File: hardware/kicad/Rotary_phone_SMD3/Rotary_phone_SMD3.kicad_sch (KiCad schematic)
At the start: 76 parts, among them J1 Barrel_Jack_PTH_Slot, J10 RJ12, J11 PINHD_1x2_Male, J12 PINHD_1x3_Male, J13 PINHD_1x2_Male, J2 PINHD_1x2_Male, J3 PINHD_1x2_Male, J4 PINHD_1x2_Male, J5 PINHD_1x2_Male, J6 PINHD_1x2_Male, J7 PINHD_1x2_Male, J8 PINHD_1x2_Male, J9 RJ12, U1 ME6211C33M5G-N, U2 ESP32-C6-WROOM-1, U3 USBLC6-2SC6, U4 ES8388, U5 AG1171, U6 AG1171

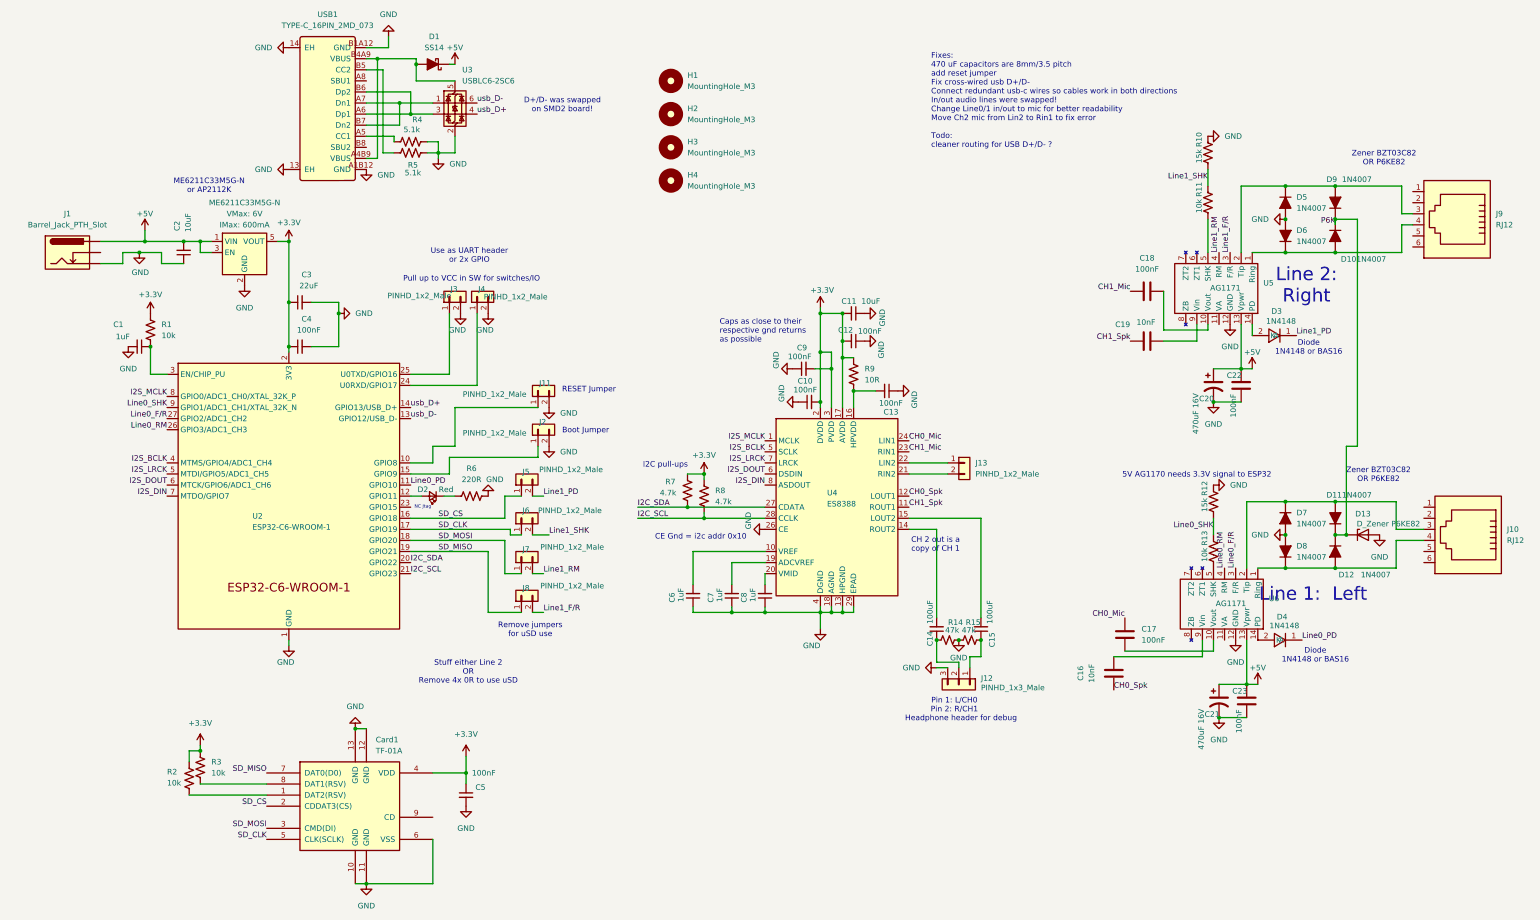
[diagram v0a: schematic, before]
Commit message: 211 recording rework, activity log, ag1170 pulse-debounce fix, SMD4 board, public docs pass
Firmware:
- ag1170: require a minimum loop-open duration (pulse_break_min_ms=15) for a
  rotary pulse to count, not just a maximum -- fixes a ~3-5ms mechanical
  contact-bounce glitch occasionally being miscounted as an extra pulse
  (confirmed live: "211" misread as "212"/"322").
- 211 recording: drop the escalating warning-beep sequence in favor of just
  ending the recording silently; default max length raised 30s -> 2min
  (still user-adjustable, capped at BOARD_RECORD_MAX_MS_MAX); recorder AGC
  with a per-block hard ceiling to stop a startup transient from clipping;
  8s trailing-silence auto-stop kept from the previous tuning pass.
- Recordings/storage lists now sort newest-first.
- sdcard: optional card-detect (CD) pin support, wired up for SMD4 (inert on
  boards without BOARD_SD_CD defined).
- New `activity` component: small ring buffer of human-readable recent
  events (calls, recordings, dial errors) for the Status page, independent
  of the raw debug log.
- webui: dial-code/guide cards moved onto the Status page; the raw debug log
  panel moved to the Diagnostics tab (Settings), next to the log-level
  controls it belongs with.
- voip: retire the voip_provisioner auto-provisioning companion service in
  favor of a plain per-board setup password (gates /api/prompt_requests for
  gen_prompt.py --sync); ships with no default SIP server/hostname baked in.
- dialplan: drop four novelty dial-code clips whose source audio never
  shipped in this checkout (burp/dial-up modem remain).

Hardware:
- Add the SMD4 KiCad project (SMD3's schematic re-routed as a 2-layer
  board); add a 3d-printed-case doc stub.
- Drop SMD3's fab-output cruft (gerbers, DRC/ERC reports, JLCImport
  libraries, BOM) from tracking -- regenerable, and JLCImport in particular
  carries machine-local absolute paths. .gitignore now covers this class of
  file for every board going forward instead of one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
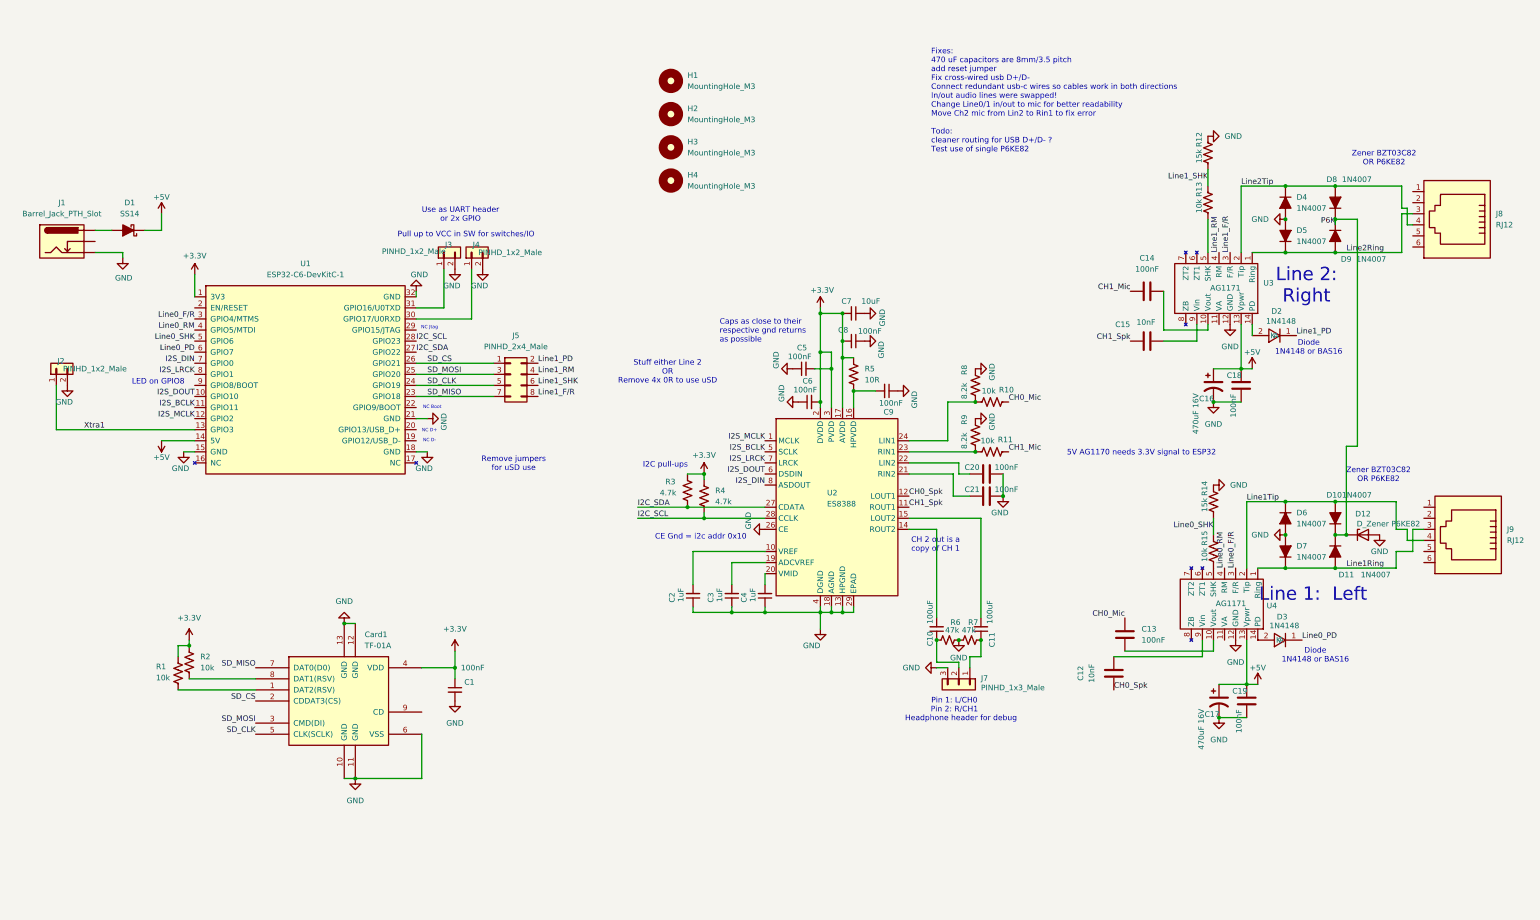
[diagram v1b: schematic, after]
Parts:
- removed C1: 1uF, Capacitor_SMD:C_0402_1005Metric, symbol PCM_SparkFun-Capacitor:C_Small
- removed C2: 10uF, Capacitor_SMD:C_0402_1005Metric, symbol PCM_SparkFun-Capacitor:C_Small
- removed C3: 22uF, PCM_SparkFun-Capacitor:C_0603_1608Metric, symbol PCM_SparkFun-Capacitor:C_Small
- removed C4: 100nF, Capacitor_SMD:C_0402_1005Metric, symbol PCM_SparkFun-Capacitor:C_Small
- removed D2: Red, PCM_SparkFun-LED:LED_0603_1608Metric_Red, symbol PCM_SparkFun-LED:LED_Red_1206
- removed J11, J13, J5, J6, J7, J8: PINHD_1x2_Male, Connector_PinHeader_2.54mm:PinHeader_1x02_P2.54mm_Vertical, symbol PCM_SL_Pin_Headers:PINHD_1x2_Male
- removed R1: 10k, Resistor_SMD:R_0402_1005Metric, symbol PCM_SparkFun-Resistor:R
- removed R4, R5: 5.1k, Resistor_SMD:R_0402_1005Metric, symbol PCM_SparkFun-Resistor:R
- removed R6: 220R, Resistor_SMD:R_0402_1005Metric, symbol PCM_SparkFun-Resistor:R
- removed U1: ME6211C33M5G-N, PCM_SparkFun-Semiconductor-Standard:SOT23-5, symbol PCM_SparkFun-Regulator:AP2112K-3.3
- removed U2: ESP32-C6-WROOM-1, PCM_Espressif:ESP32-C6-WROOM-1, symbol PCM_Espressif:ESP32-C6-WROOM-1
- removed U3: USBLC6-2SC6, Package_TO_SOT_SMD:SOT-23-6, symbol Power_Protection:USBLC6-2SC6
- removed USB1: TYPE-C_16PIN_2MD_073, JLCImport:TYPE-C_16PIN_2MD_073, symbol JLCImport:TYPE-C_16PIN_2MD_073
- added C20, C21: 100nF, Capacitor_SMD:C_0402_1005Metric, symbol Device:C
- added J5: PINHD_2x4_Male, Connector_PinHeader_2.54mm:PinHeader_2x04_P2.54mm_Vertical, symbol PCM_SL_Pin_Headers:PINHD_2x4_Male
- added R10, R11: 10k, Resistor_SMD:R_0402_1005Metric, symbol PCM_SparkFun-Resistor:R
- added R8, R9: 8.2k, Resistor_SMD:R_0402_1005Metric, symbol PCM_SparkFun-Resistor:R
- added U1: ESP32-C6-DevKitC-1, PCM_Espressif:ESP32-C6-DevKitC-1, symbol PCM_Espressif:ESP32-C6-DevKitC-1
- renumbered C5 to C1, C14 to C10, C15 to C11, C16 to C12, C17 to C13, C18 to C14, C19 to C15, C20 to C16, C21 to C17, C22 to C18, C23 to C19, C6 to C2, C7 to C3, C8 to C4, C9 to C5, C10 to C6, C11 to C7, C12 to C8, C13 to C9, D11 to D10, D12 to D11, D13 to D12, D3 to D2, D4 to D3, D5 to D4, D6 to D5, D7 to D6, D8 to D7, D9 to D8, D10 to D9, J12 to J7, J9 to J8, J10 to J9, R2 to R1, R10 to R12, R11 to R13, R12 to R14, R13 to R15, R3 to R2, R7 to R3, R8 to R4, R9 to R5, R14 to R6, R15 to R7, U4 to U2, U5 to U3, U6 to U4
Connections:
- net +3.3V: now also U1.1 (3V3)
- net +5V: now also U1.14 (5V); no longer J1.PWR
- net CH0_Mic: now also R10.1; no longer U2.24 (LIN1)
- net CH1_Mic: now also R11.1; no longer U2.23 (RIN1)
- net GND: now also C20.1, C21.1, R8.1, R9.1, U1.15 (GND), U1.18 (GND), U1.21 (GND), U1.32 (GND)
- net I2C_SCL: now also U1.28 (GPIO23)
- net I2C_SDA: now also U1.27 (GPIO22)
- net I2S_BCLK: now also U1.11 (GPIO11)
- net I2S_DIN: now also U1.7 (GPIO0)
- net I2S_DOUT: now also U1.10 (GPIO10)
- net I2S_LRCK: now also U1.8 (GPIO1)
- net I2S_MCLK: now also U1.12 (GPIO2)
- net Line0_F/R: now also U1.3 (GPIO4/MTMS)
- net Line0_PD: now also U1.6 (GPIO7)
- net Line0_RM: now also U1.4 (GPIO5/MTDI)
- net Line0_SHK: now also U1.5 (GPIO6)
- net Line1_F/R: now also J5.8
- net Line1_PD: now also J5.2
- net Line1_RM: now also J5.4
- net Line1_SHK: now also J5.6
- net SD_CLK: now also J5.5, U1.24 (GPIO19)
- net SD_CS: now also J5.1, U1.26 (GPIO21)
- net SD_MISO: now also J5.7, U1.23 (GPIO18)
- net SD_MOSI: now also J5.3, U1.25 (GPIO20)
- net Line1Tip: now reaches D10.2 (A), D6.1 (K), U4.2 (Tip)
- net Line1Tip: now also J9.4; no longer J9.3
- net Line2Tip: now reaches D4.1 (K), D8.2 (A), U3.2 (Tip)
- net Line2Tip: now also J8.4; no longer J8.3
- net Line2Ring: now reaches D5.1 (K), D9.2 (A), U3.1 (Ring)
- net Line2Ring: now also J8.3; no longer J8.4
- net at D1.2 (A): now also J1.PWR
- net at U2.22 (LIN2): now also C20.2
- net at U2.21 (RIN2): now also C21.2
- net Line1Ring: now reaches D11.2 (A), D7.1 (K), U4.1 (Ring)
- net Line1Ring: now also J9.3; no longer J9.4
- net Xtra1: now reaches J2.1
- net Xtra1: now also U1.13 (GPIO3)
- net at J4.1: now also U1.30 (GPIO17/U0RXD)
- net at J3.1: now also U1.31 (GPIO16/U0TXD)
- new net: R10.2, R8.2, U2.24 (LIN1)
- new net: R11.2, R9.2, U2.23 (RIN1)
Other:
- note added: "Fixes: 470 uF capacitors are 8mm/3.5 pitch add reset jumper Fix cross-wired usb D+/D- Connect redundant usb-c wires so cables work in both directions In/out audio lines were swapped! Change Line0/1 in/out to mic for better readability Move Ch2 mic from Lin2 to Rin1 to fix error Todo: cleaner routing for USB D+/D- ? Test use of single P6KE82"
- note added: "LED on GPIO8"
- note added: "NC Boot"
- note added: "NC D+"
- note added: "NC D-"
- note removed: "Boot Jumper"
- note removed: "D+/D- was swapped on SMD2 board!"
- note removed: "Fixes: 470 uF capacitors are 8mm/3.5 pitch add reset jumper Fix cross-wired usb D+/D- Connect redundant usb-c wires so cables work in both directions In/out audio lines were swapped! Change Line0/1 in/out to mic for better readability Move Ch2 mic from Lin2 to Rin1 to fix error Todo: cleaner routing for USB D+/D- ?"
- note removed: "ME6211C33M5G-N or AP2112K"
- note removed: "RESET Jumper"
- moved on the sheet: C1, Card1, R1, R2

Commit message: kicad: consolidate custom footprints/3D/symbols into libraries/
Move all per-project Scott.pretty, JLCImport.pretty, .3dshapes, and
.kicad_sym files into a single shared kicad/libraries/ directory.
Rename "Scott" library to "Custom" throughout. Update fp-lib-table,
sym-lib-table, .kicad_pcb, and .kicad_sch files in all 6 board
projects to resolve Custom: and JLCImport: via ${KIPRJMOD}/../libraries/.

Also fixes broken 3D model paths (hardcoded /Users/... and
_restore_backup_ references in SMD3/SMD4/AR5 PCBs).

Generated with [Devin](https://devin.ai)

Co-Authored-By: Devin <158243242+devin-ai-integration[bot]@users.noreply.github.com>
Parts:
- J8, J9: footprint Scott:RJ12_Amphenol_87180_Horizontal -> Custom:RJ12_Amphenol_87180_Horizontal
- U3, U4: footprint Scott:AG1171_SIL -> Custom:AG1171_SIL; symbol Scott_Symbol_Library:AG1171_SIL -> Custom_Symbol_Library:AG1171_SIL
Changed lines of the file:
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@@
 			)
 		)
-		(property "Footprint" "Scott:RJ12_Amphenol_87180_Horizontal"
+		(property "Footprint" "Custom:RJ12_Amphenol_87180_Horizontal"
 			(at 364.49 67.945 90)
 			(hide yes)
@@
 			)
 		)
-		(property "Footprint" "Scott:RJ12_Amphenol_87180_Horizontal"
+		(property "Footprint" "Custom:RJ12_Amphenol_87180_Horizontal"
 			(at 367.03 140.335 90)
 			(hide yes)
@@
 	)
 	(symbol
-		(lib_id "Scott_Symbol_Library:AG1171_SIL")
+		(lib_id "Custom_Symbol_Library:AG1171_SIL")
 		(at 308.61 160.02 180)
 		(unit 1)
@@
 			)
 		)
-		(property "Footprint" "Scott:AG1171_SIL"
+		(property "Footprint" "Custom:AG1171_SIL"
 			(at 308.61 160.02 0)
 			(hide yes)
@@
 	)
 	(symbol
-		(lib_id "Scott_Symbol_Library:AG1171_SIL")
+		(lib_id "Custom_Symbol_Library:AG1171_SIL")
 		(at 307.34 87.63 180)
 		(unit 1)
@@
 			)
 		)
-		(property "Footprint" "Scott:AG1171_SIL"
+		(property "Footprint" "Custom:AG1171_SIL"
 			(at 307.34 87.63 0)
 			(hide yes)
